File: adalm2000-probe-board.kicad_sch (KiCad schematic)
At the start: 14 parts, among them J1 ADALM200 INPUT, J2 MODULE OUTPUT, J3 Ch1, J4 Ch2, J5 V+/W1, J6 V-/W2, SW1 SW_CH1_CPL, SW2 SW_CH1_GND_REF, SW3 SW_CH2_CPL, SW4 SW_CH2_GND_REF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

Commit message: Initial PCB design
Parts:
- added J7: V+/V- OUT, digikey-footprints:PinHeader_1x3_P2.54_Drill1.1mm, symbol dk_Rectangular-Connectors-Headers-Male-Pins:61300311121
- C1, C2: value C -> 0.1uF; footprint (none) -> Capacitor_SMD:C_0805_2012Metric
- J1: footprint Connector_IDC:IDC-Header_2x15_P2.54mm_Vertical -> Connector_IDC:IDC-Header_2x15_P2.54mm_Horizontal
- J2: footprint Connector_IDC:IDC-Header_2x15_P2.54mm_Vertical -> Jonnes Library:IDC-Header_2x15_P2.54mm_Horizontal - Pin 1 on left from front view
- J3: value Ch1 -> CH1; footprint (none) -> w_conn_rf:bnc_90_1-1337543-0
- J4: value Ch2 -> CH2; footprint (none) -> w_conn_rf:bnc_90_1-1337543-0
- J5, J6: footprint (none) -> w_conn_rf:bnc_90_1-1337543-0
- SW1, SW2, SW3, SW4, SW5, SW6: footprint (none) -> KiCad:SS12D00G3
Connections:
- net GND4: now also J7.3
- net V+: now also J7.1
- net V-: now also J7.2
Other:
- note added: "OUT"
- company: (none) -> Eng. Jonnes Nascimento
- title: (none) -> ADALM2000 Probe Board
- moved on the sheet: C1, C2, J1, J2, J3, J4, J5, J6, SW1, SW2, SW3, SW4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

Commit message: Initial PCB design
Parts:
- J1: footprint Connector_IDC:IDC-Header_2x15_P2.54mm_Horizontal -> Jonnes Library:PinSocket_2x15_P2.54mm_Horizontal
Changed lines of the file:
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@@
       (effects (font (size 1.27 1.27)) (justify left))
     )
-    (property "Footprint" "Connector_IDC:IDC-Header_2x15_P2.54mm_Horizontal" (id 2) (at 153.67 59.69 0)
+    (property "Footprint" "Jonnes Library:PinSocket_2x15_P2.54mm_Horizontal" (id 2) (at 153.67 59.69 0)
       (effects (font (size 1.27 1.27)) hide)
     )
@@
     )
     (path "/01e8a7f1-e668-442f-9994-925c867ee32b"
-      (reference "J1") (unit 1) (value "ADALM200 INPUT") (footprint "Connector_IDC:IDC-Header_2x15_P2.54mm_Horizontal")
+      (reference "J1") (unit 1) (value "ADALM200 INPUT") (footprint "Jonnes Library:PinSocket_2x15_P2.54mm_Horizontal")
     )
     (path "/d2fc562b-36d8-46a5-80f9-e350584d36cd"

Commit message: Adding images and configuring board layers
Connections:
- net 1-: now also J3.2 (Ext), SW2.2 (B)
- net 2-: now also J4.2 (Ext), SW4.2 (B)
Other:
- company: Eng. Jonnes Nascimento -> RetroLabs - Eng. Jonnes Nascimento
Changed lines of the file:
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@@
     (title "ADALM2000 Probe Board")
     (date "2022-11-30")
-    (company "Eng. Jonnes Nascimento")
+    (company "RetroLabs - Eng. Jonnes Nascimento")
     (comment 1 "Others: Blue mask with white silk")
     (comment 2 "Layers: 4 (2 surfaces and 2 GND central layers)")
@@
   (junction (at 81.28 100.33) (diameter 0) (color 0 0 0 0)
   )
+  (junction (at 86.36 57.15) (diameter 0) (color 0 0 0 0)
+  )
   (junction (at 81.28 49.53) (diameter 0) (color 0 0 0 0)
   )
+  (junction (at 86.36 107.95) (diameter 0) (color 0 0 0 0)
+  )
   (wire (pts (xy 156.21 97.79) (xy 156.21 106.68))
     (stroke (width 0) (type default) (color 0 0 0 0))
@@
     (stroke (width 0) (type default) (color 0 0 0 0))
   )
+  (wire (pts (xy 86.36 107.95) (xy 96.52 107.95))
+    (stroke (width 0) (type default) (color 0 0 0 0))
+  )
   (wire (pts (xy 62.23 154.94) (xy 77.47 154.94))
     (stroke (width 0) (type default) (color 0 0 0 0))
@@
     (stroke (width 0) (type default) (color 0 0 0 0))
   )
+  (wire (pts (xy 86.36 57.15) (xy 86.36 58.42))
+    (stroke (width 0) (type default) (color 0 0 0 0))
+  )
   (wire (pts (xy 158.75 97.79) (xy 158.75 106.68))
     (stroke (width 0) (type default) (color 0 0 0 0))
@@
     (stroke (width 0) (type default) (color 0 0 0 0))
   )
-  (wire (pts (xy 86.36 54.61) (xy 86.36 58.42))
+  (wire (pts (xy 86.36 54.61) (xy 86.36 57.15))
     (stroke (width 0) (type default) (color 0 0 0 0))
   )
@@
     (stroke (width 0) (type default) (color 0 0 0 0))
   )
-  (wire (pts (xy 86.36 105.41) (xy 86.36 109.22))
+  (wire (pts (xy 86.36 105.41) (xy 86.36 107.95))
     (stroke (width 0) (type default) (color 0 0 0 0))
   )
@@
     (stroke (width 0) (type default) (color 0 0 0 0))
   )
+  (wire (pts (xy 86.36 107.95) (xy 86.36 109.22))
+    (stroke (width 0) (type default) (color 0 0 0 0))
+  )
   (wire (pts (xy 63.5 54.61) (xy 68.58 54.61))
     (stroke (width 0) (type default) (color 0 0 0 0))
@@
   )
   (wire (pts (xy 226.06 50.8) (xy 236.22 50.8))
+    (stroke (width 0) (type default) (color 0 0 0 0))
+  )
+  (wire (pts (xy 86.36 57.15) (xy 96.52 57.15))
     (stroke (width 0) (type default) (color 0 0 0 0))
   )
@@
     )
   )
+  (global_label "2-" (shape input) (at 96.52 107.95 0) (fields_autoplaced)
+    (effects (font (size 1.27 1.27)) (justify left))
+    (property "Intersheet References" "${INTERSHEET_REFS}" (id 0) (at 101.715 108.0294 0)
+      (effects (font (size 1.27 1.27)) (justify left) hide)
+    )
+  )
   (global_label "2-" (shape input) (at 138.43 129.54 270) (fields_autoplaced)
     (effects (font (size 1.27 1.27)) (justify right))
@@
       (effects (font (size 1.27 1.27)) (justify right) hide)
     )
+  )
+  (global_label "1-" (shape input) (at 96.52 57.15 0) (fields_autoplaced)
+    (effects (font (size 1.27 1.27)) (justify left))
+    (property "Intersheet References" "${INTERSHEET_REFS}" (id 0) (at 101.715 57.0706 0)
+      (effects (font (size 1.27 1.27)) (justify right) hide)
+    )

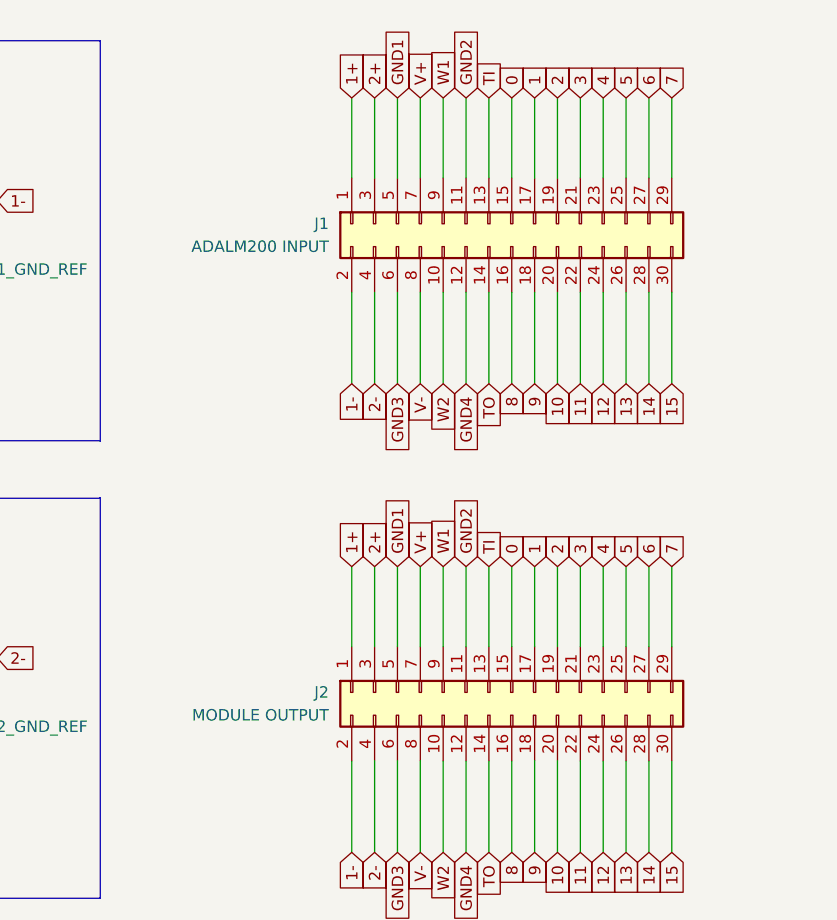
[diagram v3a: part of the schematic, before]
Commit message: Board initial routing
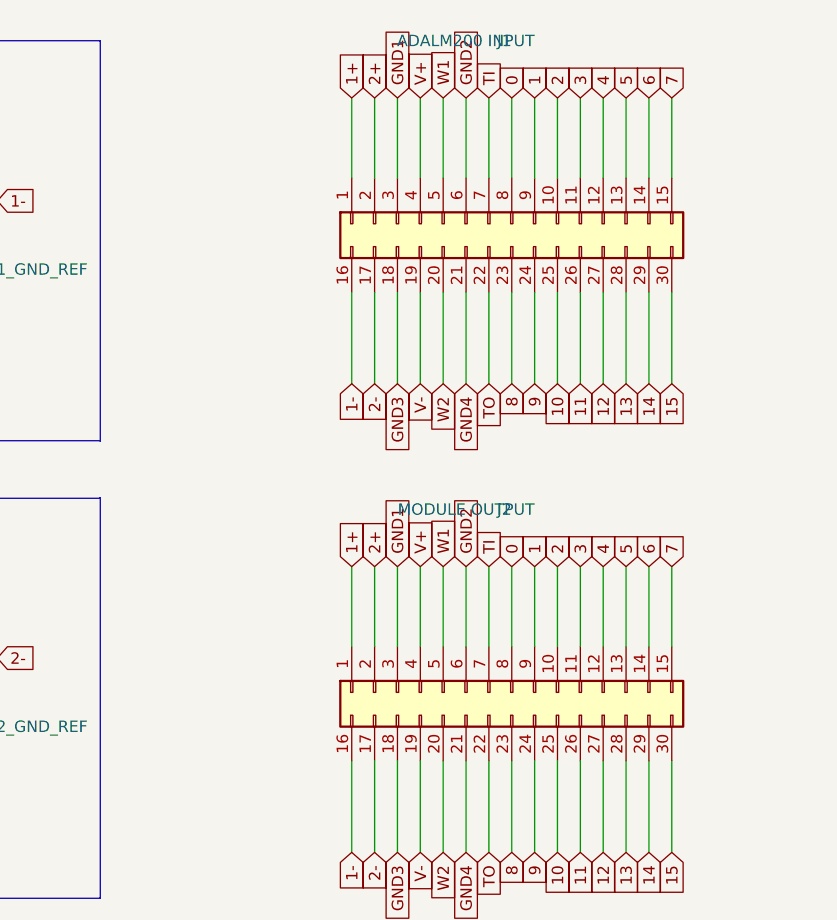
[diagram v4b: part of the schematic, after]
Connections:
- net 0: now also J1.8 (Pin_8), J2.8 (Pin_8); no longer J1.15 (Pin_15), J2.15 (Pin_15)
- net 1: now also J1.9 (Pin_9), J2.9 (Pin_9); no longer J1.17 (Pin_17), J2.17 (Pin_17)
- net 1-: now also J1.16 (Pin_16), J2.16 (Pin_16); no longer J1.2 (Pin_2), J2.2 (Pin_2)
- net 10: now also J1.25 (Pin_25), J2.25 (Pin_25); no longer J1.20 (Pin_20), J2.20 (Pin_20)
- net 11: now also J1.26 (Pin_26), J2.26 (Pin_26); no longer J1.22 (Pin_22), J2.22 (Pin_22)
- net 12: now also J1.27 (Pin_27), J2.27 (Pin_27); no longer J1.24 (Pin_24), J2.24 (Pin_24)
- net 13: now also J1.28 (Pin_28), J2.28 (Pin_28); no longer J1.26 (Pin_26), J2.26 (Pin_26)
- net 14: now also J1.29 (Pin_29), J2.29 (Pin_29); no longer J1.28 (Pin_28), J2.28 (Pin_28)
- net 2: now also J1.10 (Pin_10), J2.10 (Pin_10); no longer J1.19 (Pin_19), J2.19 (Pin_19)
- net 2+: now also J1.2 (Pin_2), J2.2 (Pin_2); no longer J1.3 (Pin_3), J2.3 (Pin_3)
- net 2-: now also J1.17 (Pin_17), J2.17 (Pin_17); no longer J1.4 (Pin_4), J2.4 (Pin_4)
- net 3: now also J1.11 (Pin_1), J2.11 (Pin_11); no longer J1.21 (Pin_21), J2.21 (Pin_21)
- net 4: now also J1.12 (Pin_12), J2.12 (Pin_12); no longer J1.23 (Pin_23), J2.23 (Pin_23)
- net 5: now also J1.13 (Pin_13), J2.13 (Pin_13); no longer J1.25 (Pin_25), J2.25 (Pin_25)
- net 6: now also J1.14 (Pin_14), J2.14 (Pin_14); no longer J1.27 (Pin_27), J2.27 (Pin_27)
- net 7: now also J1.15 (Pin_15), J2.15 (Pin_15); no longer J1.29 (Pin_29), J2.29 (Pin_29)
- net 8: now also J1.23 (Pin_23), J2.23 (Pin_23); no longer J1.16 (Pin_16), J2.16 (Pin_16)
- net 9: now also J1.24 (Pin_24), J2.24 (Pin_24); no longer J1.18 (Pin_18), J2.18 (Pin_18)
- net GND1: now also J1.3 (Pin_3), J2.3 (Pin_3); no longer J1.5 (Pin_5), J2.5 (Pin_5)
- net GND2: now also J1.6 (Pin_6), J2.6 (Pin_6); no longer J1.11 (Pin_11), J2.11 (Pin_11)
- net GND3: now also J1.18 (Pin_18), J2.18 (Pin_18); no longer J1.6 (Pin_6), J2.6 (Pin_6)
- net GND4: now also J1.21 (Pin_21), J2.21 (Pin_21); no longer J1.12 (Pin_12), J2.12 (Pin_12)
- net TI: now also J1.7 (Pin_7), J2.7 (Pin_7); no longer J1.13 (Pin_13), J2.13 (Pin_13)
- net TO: now also J1.22 (Pin_22), J2.22 (Pin_22); no longer J1.14 (Pin_14), J2.14 (Pin_14)
- net V+: now also J1.4 (Pin_4), J2.4 (Pin_4); no longer J1.7 (Pin_7), J2.7 (Pin_7)
- net V-: now also J1.19 (Pin_19), J2.19 (Pin_19); no longer J1.8 (Pin_8), J2.8 (Pin_8)
- net W1: now also J1.5 (Pin_5), J2.5 (Pin_5); no longer J1.9 (Pin_9), J2.9 (Pin_9)
- net W2: now also J1.20 (Pin_20), J2.20 (Pin_20); no longer J1.10 (Pin_10), J2.10 (Pin_10)
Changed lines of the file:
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@@
     )
   )
-  (symbol (lib_id "Connector_Generic:Conn_02x15_Odd_Even") (at 153.67 59.69 90) (mirror x) (unit 1)
-    (in_bom yes) (on_board yes) (fields_autoplaced)
-    (property "Reference" "J1" (id 0) (at 133.35 59.6899 90)
-      (effects (font (size 1.27 1.27)) (justify left))
-    )
-    (property "Value" "ADALM200 INPUT" (id 1) (at 133.35 62.2299 90)
-      (effects (font (size 1.27 1.27)) (justify left))
-    )
-    (property "Footprint" "Jonnes Library:PinSocket_2x15_P2.54mm_Horizontal" (id 2) (at 153.67 59.69 0)
+  (symbol (lib_name "Conn_02x15_Odd_Even_1") (lib_id "Connector_Generic:Conn_02x15_Odd_Even") (at 153.67 59.69 90) (mirror x) (unit 1)
+    (in_bom yes) (on_board yes) (fields_autoplaced)
+    (property "Reference" "J1" (id 0) (at 153.6699 39.37 90)
+      (effects (font (size 1.27 1.27)) (justify left))
+    )
+    (property "Value" "ADALM200 INPUT" (id 1) (at 156.2099 39.37 90)
+      (effects (font (size 1.27 1.27)) (justify left))
+    )
+    (property "Footprint" "Jonnes Library:PinSocket_2x15_P2.54mm_Horizontal" (id 2) (at 175.26 59.69 0)
       (effects (font (size 1.27 1.27)) hide)
     )
@@
     )
     (pin "1")
+    (pin "20")
+    (pin "6")
+    (pin "21")
+    (pin "7")
+    (pin "22")
+    (pin "8")
+    (pin "23")
+    (pin "9")
+    (pin "24")
     (pin "10")
+    (pin "16")
+    (pin "25")
     (pin "11")
+    (pin "26")
     (pin "12")
+    (pin "27")
     (pin "13")
+    (pin "28")
     (pin "14")
+    (pin "29")
     (pin "15")
-    (pin "16")
+    (pin "2")
+    (pin "30")
     (pin "17")
+    (pin "3")
     (pin "18")
+    (pin "4")
     (pin "19")
-    (pin "2")
-    (pin "20")
-    (pin "21")
-    (pin "22")
-    (pin "23")
-    (pin "24")
-    (pin "25")
-    (pin "26")
-    (pin "27")
-    (pin "28")
-    (pin "29")
-    (pin "3")
-    (pin "30")
-    (pin "4")
     (pin "5")
-    (pin "6")
-    (pin "7")
-    (pin "8")
-    (pin "9")
   )
   (symbol (lib_id "Switch:SW_SPDT") (at 58.42 102.87 0) (unit 1)
@@
   (symbol (lib_id "Connector_Generic:Conn_02x15_Odd_Even") (at 153.67 111.76 90) (mirror x) (unit 1)
     (in_bom yes) (on_board yes) (fields_autoplaced)
-    (property "Reference" "J2" (id 0) (at 133.35 111.7599 90)
-      (effects (font (size 1.27 1.27)) (justify left))
-    )
-    (property "Value" "MODULE OUTPUT" (id 1) (at 133.35 114.2999 90)
-      (effects (font (size 1.27 1.27)) (justify left))
-    )
-    (property "Footprint" "Jonnes Library:IDC-Header_2x15_P2.54mm_Horizontal - Pin 1 on left from front view" (id 2) (at 153.67 111.76 0)
+    (property "Reference" "J2" (id 0) (at 153.6699 91.44 90)
+      (effects (font (size 1.27 1.27)) (justify left))
+    )
+    (property "Value" "MODULE OUTPUT" (id 1) (at 156.2099 91.44 90)
+      (effects (font (size 1.27 1.27)) (justify left))
+    )
+    (property "Footprint" "Jonnes Library:IDC-Header_2x15_P2.54mm_Horizontal - Pin 1 on left from front view" (id 2) (at 175.26 113.03 0)
       (effects (font (size 1.27 1.27)) hide)
     )
@@
     )
     (pin "1")
+    (pin "20")
+    (pin "6")
+    (pin "21")
+    (pin "7")
+    (pin "22")
+    (pin "8")
+    (pin "23")
+    (pin "9")
+    (pin "24")
     (pin "10")
+    (pin "16")
+    (pin "25")
     (pin "11")
+    (pin "26")
     (pin "12")
+    (pin "27")
     (pin "13")
+    (pin "28")
     (pin "14")
+    (pin "29")
     (pin "15")
-    (pin "16")
+    (pin "2")
+    (pin "30")
     (pin "17")
+    (pin "3")
     (pin "18")
+    (pin "4")
     (pin "19")
-    (pin "2")
-    (pin "20")
-    (pin "21")
-    (pin "22")
-    (pin "23")
-    (pin "24")
-    (pin "25")
-    (pin "26")
-    (pin "27")
-    (pin "28")
-    (pin "29")
-    (pin "3")
-    (pin "30")
-    (pin "4")
     (pin "5")
-    (pin "6")
-    (pin "7")
-    (pin "8")
-    (pin "9")
   )
   (symbol (lib_id "Switch:SW_SPDT") (at 220.98 102.87 0) (mirror y) (unit 1)
